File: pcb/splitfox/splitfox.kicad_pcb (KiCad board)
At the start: 2 copper layers, 255.8 x 122.5 mm, 137 parts, among them CN1 S7B-ZR-SM4A-TF(LF)(SN)_C51187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, CN2 S7B-ZR-SM4A-TF(LF)(SN)_C51187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, SW1 TS24CA, SW2 SS-12D07-L5-B, SW3 GT-TC152A-H085-L1, SW4 GT-TC152A-H085-L1, SW5 GT-TC152A-H085-L1, SW6 GT-TC152A-H085-L1, SW7 GT-TC152A-H085-L1, SW8 GT-TC152A-H085-L1, U1 RP2040, U2 SN74LV1T34DBVR, U3 W25Q128JVS, U4 XC6206PxxxMR-Regulator_Linear, U5 USBLC6-2SC6, Y1 12MHz

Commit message: NG | Splitfox PCB Placement
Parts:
- C13: value 10uF -> 100uF
- LOGO1, LOGO2: moved to F.Cu
- moved C37 247.4 mm to (272.1, 101.2)
- moved C48 227.5 mm to (176.5, 140.2)
- moved C35 227.4 mm to (210.3, 137.3)
- moved C28 225.5 mm to (193.4, 129.7)
- moved C30 225.4 mm to (255.2, 93.6)
- moved C50 220.5 mm to (243.0, 96.6)
- moved C44 215.3 mm to (274.2, 64.2), turned to 0 degrees
- moved C47 212.9 mm to (108.6, 137.3)
- moved C41 210.2 mm to (159.4, 132.5)
- moved LED12 209.7 mm to (269.6, 97.3), turned to 0 degrees
- moved C34 209.2 mm to (142.4, 140.2)
- moved LED10 204.2 mm to (207.9, 133.5), turned to 0 degrees
- moved LED23 203.7 mm to (174.0, 136.3), turned to 0 degrees
- moved C51 203.2 mm to (252.7, 64.2), turned to 0 degrees
- moved LED19 202.8 mm to (272.3, 67.9)
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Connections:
- CN2 pad 8: unconnected-(CN2-Pad8) -> GND
- CN2 pad 9: unconnected-(CN2-Pad9) -> GND
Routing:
- added copper zone on B.Cu, net +1V1
- added copper zone on B.Cu, net +3V3

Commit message: NG | Ready for routing
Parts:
- moved C20 0.40 mm to (154.1, 124.7)

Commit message: NG | SplitFox PCB, Redid body cad
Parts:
- C13: value 100uF -> 100nF
- C6, C7: value 30pF -> 15pF
- LOGO1: moved to B.Cu
- LOGO2: footprint PicoFoxpretty:picofox -> PicoFoxpretty:picofox_small
- moved LOGO2 160.2 mm to (117.0, 126.4)
- moved LOGO1 66.5 mm to (105.0, 115.0), turned to 180 degrees
- moved R3 46.9 mm to (159.3, 122.5), turned to 180 degrees
- moved R4 46.0 mm to (159.3, 121.5), turned to 180 degrees
- moved C39 9.01 mm to (174.7, 76.2)
- moved C38 9.00 mm to (230.9, 64.8)
- moved C51 8.96 mm to (260.1, 69.3)
- moved C52 8.92 mm to (201.4, 63.9)
- moved C37 8.19 mm to (269.1, 93.5), turned to 0 degrees
- moved C53 8.04 mm to (189.4, 41.7), turned to 0 degrees
- moved C49 8.03 mm to (184.0, 100.5), turned to 0 degrees
- moved C36 8.02 mm to (210.8, 88.2), turned to 0 degrees
- moved C50 8.01 mm to (240.3, 89.1), turned to 0 degrees
- moved C32 6.37 mm to (189.7, 77.4), turned to 180 degrees
- moved C45 6.36 mm to (216.5, 65.0), turned to 180 degrees
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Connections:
- CH10 pad 1: /GPIO10 -> /GPIO11
- CH11 pad 1: /GPIO16 -> /GPIO18
- CH12 pad 1: /GPIO9 -> /GPIO10
- CH4 pad 1: /GPIO13 -> /GPIO9
- CH6 pad 1: /GPIO12 -> /GPIO13
- CH7 pad 1: /GPIO18 -> /GPIO16
- CH8 pad 1: /GPIO11 -> /GPIO12
- CN1 pad 8: unconnected-(CN1-Pad8) -> GND
- CN1 pad 9: unconnected-(CN1-Pad9) -> GND
- FPC1 pad 31: unconnected-(FPC1-Pad31) -> GND
- FPC1 pad 32: unconnected-(FPC1-Pad32) -> GND
- LED12 pad 3: Net-(LED12-DIN) -> Net-(LED10-DOUT)
- LED17 pad 2: Net-(LED17-DOUT) -> Net-(LED14-DIN)
- LED17 pad 3: Net-(LED10-DOUT) -> Net-(LED17-DIN)
- LED18 pad 2: Net-(LED18-DOUT) -> Net-(LED11-DIN)
- LED18 pad 3: Net-(LED11-DOUT) -> Net-(LED18-DIN)
- LED19 pad 3: Net-(LED12-DOUT) -> Net-(LED19-DIN)
- LED20 pad 2: Net-(LED20-DOUT) -> Net-(LED13-DIN)
- LED20 pad 3: Net-(LED13-DOUT) -> Net-(LED20-DIN)
- LED21 pad 2: Net-(LED21-DOUT) -> LED_DATA_END
- LED21 pad 3: Net-(LED14-DOUT) -> Net-(LED21-DIN)
- LED24 pad 2: Net-(LED24-DOUT) -> Net-(LED17-DIN)
- LED24 pad 3: Net-(LED17-DOUT) -> Net-(LED24-DIN)
- LED25 pad 2: Net-(LED25-DOUT) -> Net-(LED18-DIN)
- LED25 pad 3: Net-(LED18-DOUT) -> Net-(LED25-DIN)
- LED26 pad 2: Net-(LED26-DOUT) -> Net-(LED19-DIN)
- LED26 pad 3: Net-(LED19-DOUT) -> Net-(LED26-DIN)
- LED27 pad 2: Net-(LED27-DOUT) -> Net-(LED20-DIN)
- LED27 pad 3: Net-(LED20-DOUT) -> Net-(LED27-DIN)
- LED28 pad 2: LED_DATA_END -> Net-(LED21-DIN)
- LED28 pad 3: Net-(LED21-DOUT) -> Net-(LED19-DOUT)
- LED4 pad 2: Net-(LED11-DIN) -> Net-(LED24-DIN)
- LED4 pad 3: Net-(LED24-DOUT) -> Net-(LED11-DOUT)
- LED5 pad 2: Net-(LED12-DIN) -> Net-(LED25-DIN)
- LED5 pad 3: Net-(LED25-DOUT) -> Net-(LED12-DOUT)
- LED6 pad 2: Net-(LED13-DIN) -> Net-(LED26-DIN)
- LED6 pad 3: Net-(LED26-DOUT) -> Net-(LED13-DOUT)
- LED7 pad 2: Net-(LED14-DIN) -> Net-(LED27-DIN)
- LED7 pad 3: Net-(LED27-DOUT) -> Net-(LED14-DOUT)
- SW1 pad 1: unconnected-(SW1-Pad1) -> GND
- SW1 pad 2: (no net) -> GND
- SW2 pad EH: unconnected-(SW2-PadEH) -> GND
- SW3 pad 2: unconnected-(SW3-B-Pad2) -> /GPIO23
- SW3 pad 3: unconnected-(SW3-C-Pad3) -> GND
- SW4 pad 2: unconnected-(SW4-B-Pad2) -> /GPIO6
- SW4 pad 3: unconnected-(SW4-C-Pad3) -> GND
- SW5 pad 2: unconnected-(SW5-B-Pad2) -> /GPIO24
- SW5 pad 3: unconnected-(SW5-C-Pad3) -> GND
- SW6 pad 2: unconnected-(SW6-B-Pad2) -> /GPIO7
- SW6 pad 3: unconnected-(SW6-C-Pad3) -> GND
- SW7 pad 2: unconnected-(SW7-B-Pad2) -> /GPIO25
- SW7 pad 3: unconnected-(SW7-C-Pad3) -> GND
- SW8 pad 2: unconnected-(SW8-B-Pad2) -> /GPIO8
- SW8 pad 3: unconnected-(SW8-C-Pad3) -> GND
- USB1 pad 5: unconnected-(USB1-Pad5) -> GND
- USB1 pad 6: unconnected-(USB1-Pad6) -> GND
- USB1 pad 7: unconnected-(USB1-Pad7) -> GND
- USB1 pad 8: unconnected-(USB1-Pad8) -> GND
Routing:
- net +5V: track 0.00 -> 921.2 mm, vias 0 -> 18
- net /GPIO25: track 0.00 -> 204.2 mm
- net /GPIO24: track 0.00 -> 194.7 mm
- net /GPIO23: track 0.00 -> 189.9 mm
- net GND: track 0.00 -> 185.6 mm, vias 0 -> 171
- net /GPIO8: track 0.00 -> 172.9 mm
- net /GPIO18: track 0.00 -> 159.4 mm
- net /GPIO7: track 0.00 -> 159.0 mm
- net /GPIO22: track 0.00 -> 149.0 mm
- net /GPIO6: track 0.00 -> 145.4 mm
- net /GPIO21: track 0.00 -> 140.1 mm
- net /GPIO13: track 0.00 -> 139.2 mm
- net Net-(LED19-DOUT): track 0.00 -> 118.0 mm
- net /GPIO5: track 0.00 -> 117.9 mm
- net /~{USB_BOOT}: track 0.00 -> 111.3 mm, vias 0 -> 4
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- added copper zone on F.Cu, net +3V3
- added copper zone on B.Cu, net GND
- added copper zone on F.Cu, net GND

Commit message: NG | It's done-ish, pcb tweaks, assembly
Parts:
- moved F1 2.77 mm to (151.2, 78.3)
- moved USB1 2.57 mm to (155.3, 69.7)
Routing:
- net LED_DATA_END: track 106.8 -> 111.5 mm
- net Net-(USB1-D-): track 54.4 -> 51.9 mm
- net Net-(USB1-D+): track 55.7 -> 53.1 mm
- net GND: track 185.6 -> 187.8 mm
- net /GPIO8: track 172.9 -> 171.3 mm, vias 0 -> 2
- net /GPIO6: track 145.4 -> 143.9 mm
- net /GPIO5: track 117.9 -> 116.5 mm
- net /GPIO7: track 159.0 -> 157.6 mm
- net /~{USB_BOOT}: track 111.3 -> 110.5 mm
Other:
- outline, holes or cut-outs redrawn

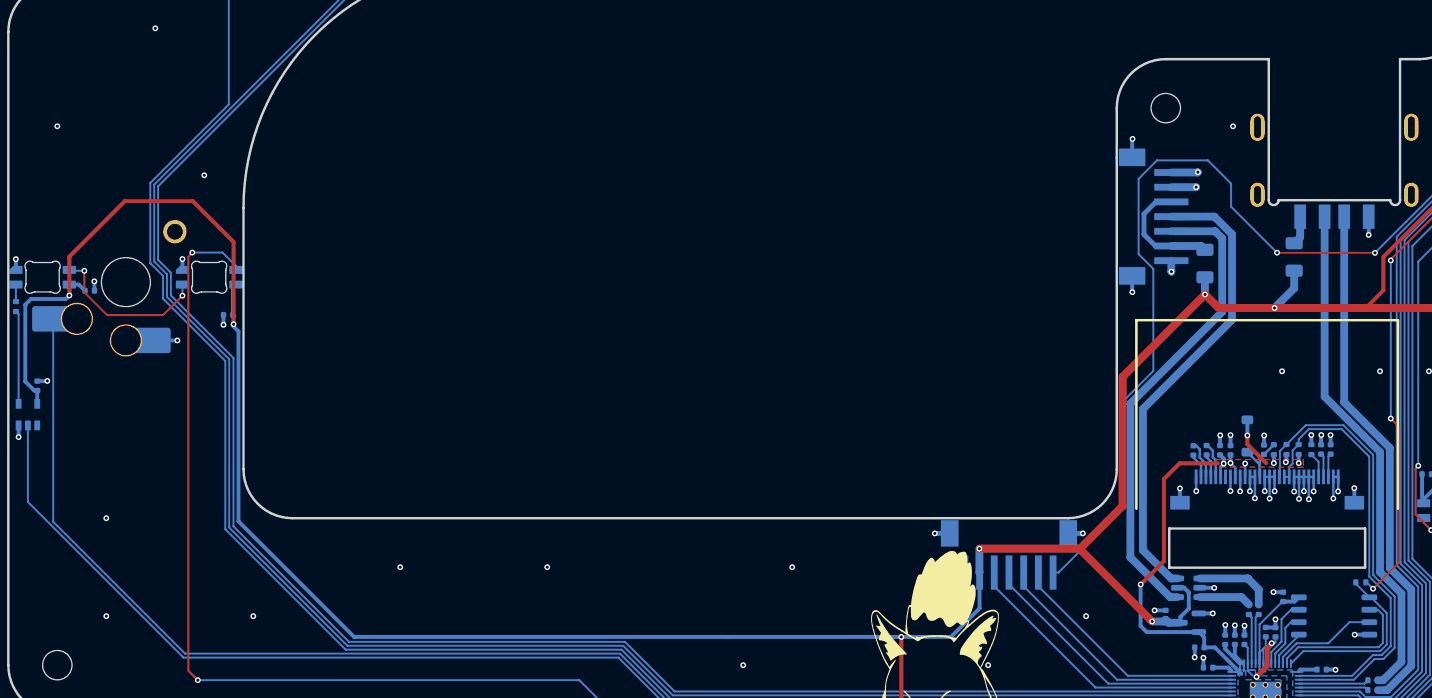
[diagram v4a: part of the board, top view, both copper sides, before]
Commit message: NG | ESD/EMI caps, USB C flash port
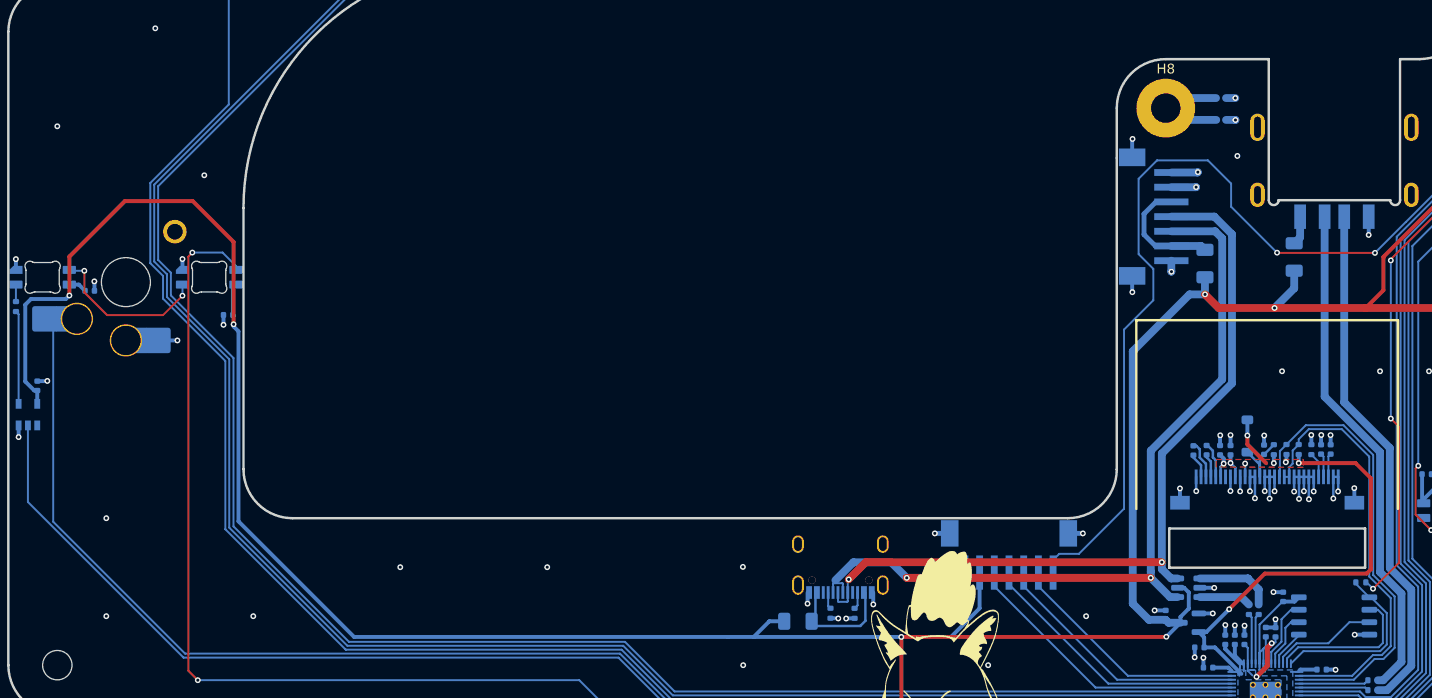
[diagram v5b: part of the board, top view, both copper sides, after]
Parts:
- added C54: 100nF, Capacitor_SMD:C_0402_1005Metric, B.Cu at (143.8, 64.3)
- added F3: 500mA, Fuse:Fuse_1206_3216Metric, B.Cu at (100.6, 115.5)
- added R12: 4.7M, Resistor_SMD:R_0402_1005Metric, B.Cu at (143.8, 62.1)
- added R13: 5k1, Resistor_SMD:R_0402_1005Metric, B.Cu at (103.9, 114.7)
- added R14: 5k1, Resistor_SMD:R_0402_1005Metric, B.Cu at (106.4, 114.7)
- added USBC1: TYPE-C-31-M-12, easyeda:USB-C_SMD-TYPE-C-31-M-12, B.Cu at (104.9, 110.1)
- H8: value MountingHole -> MountingHole_Pad; footprint MountingHole:MountingHole_3mm -> MountingHole:MountingHole_3mm_Pad
- moved LOGO1 17.8 mm to (87.2, 115.6)
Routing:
- net D_USB_P: track 47.7 -> 83.0 mm, vias 0 -> 2
- net D_USB_N: track 48.4 -> 83.2 mm, vias 0 -> 2
- net +5V: track 920.9 -> 937.5 mm, vias 18 -> 17
- net VBUS_C: track 0.00 -> 11.9 mm
- net Net-(C54-Pad1): track 0.00 -> 11.2 mm
- net +3V3: track 90.0 -> 99.1 mm
- net GND: track 187.8 -> 195.6 mm, vias 171 -> 177
- net Net-(USBC1-CC2): track 0.00 -> 1.74 mm
- net Net-(USBC1-CC1): track 0.00 -> 1.70 mm
- net LED_DATA_END: track 111.5 -> 112.4 mm
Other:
- board text added: "FLASH"
- board text added: "USB"
- board text added: "WASD"

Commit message: NG | v1.1 SplitFox PCB - old crystal setup test
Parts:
- C6, C7: value 15pF -> 30pF
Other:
- board text added: "SplitFox v1.1"
- board text removed: "SplitFox v1"
